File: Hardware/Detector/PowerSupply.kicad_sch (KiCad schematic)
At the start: 3 parts

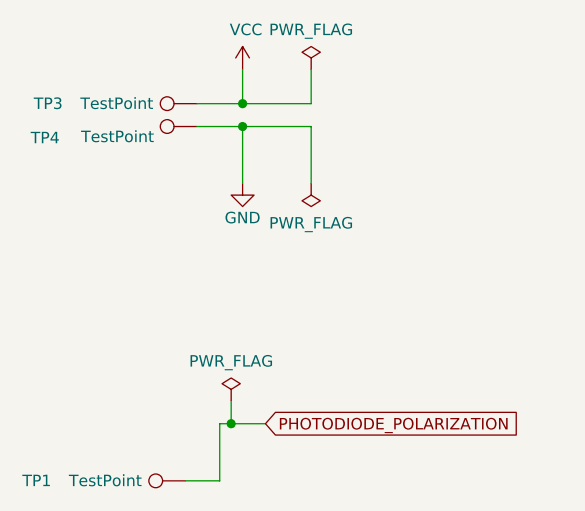
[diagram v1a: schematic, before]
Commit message: further implementation of low cost version
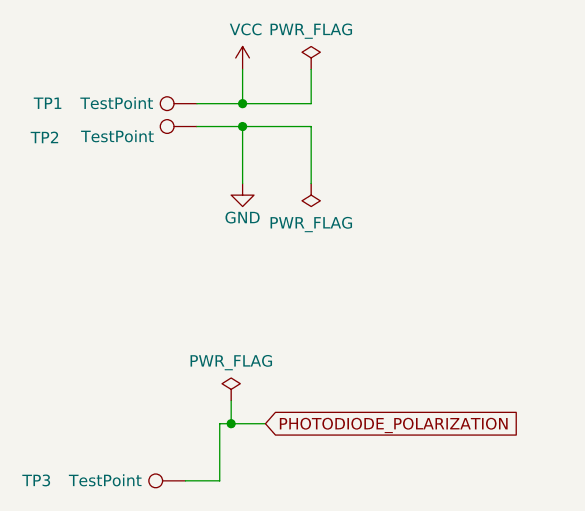
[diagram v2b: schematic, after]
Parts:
- renumbered TP3 to TP1, TP4 to TP2, TP1 to TP3
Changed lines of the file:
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@@
   (symbol (lib_id "power:VCC") (at 95.25 63.5 0) (unit 1)
     (in_bom yes) (on_board yes)
-    (property "Reference" "#PWR021" (id 0) (at 95.25 67.31 0)
+    (property "Reference" "#PWR020" (id 0) (at 95.25 67.31 0)
       (effects (font (size 1.27 1.27)) hide)
     )
@@
   (symbol (lib_id "power:PWR_FLAG") (at 93.98 100.33 0) (unit 1)
     (in_bom yes) (on_board yes)
-    (property "Reference" "#FLG02" (id 0) (at 93.98 98.425 0)
+    (property "Reference" "#FLG04" (id 0) (at 93.98 98.425 0)
       (effects (font (size 1.27 1.27)) hide)
     )
@@
   (symbol (lib_id "power:PWR_FLAG") (at 102.87 63.5 0) (unit 1)
     (in_bom yes) (on_board yes)
-    (property "Reference" "#FLG03" (id 0) (at 102.87 61.595 0)
+    (property "Reference" "#FLG02" (id 0) (at 102.87 61.595 0)
       (effects (font (size 1.27 1.27)) hide)
     )
@@
   (symbol (lib_id "power:PWR_FLAG") (at 102.87 76.2 180) (unit 1)
     (in_bom yes) (on_board yes)
-    (property "Reference" "#FLG04" (id 0) (at 102.87 78.105 0)
+    (property "Reference" "#FLG03" (id 0) (at 102.87 78.105 0)
       (effects (font (size 1.27 1.27)) hide)
     )
@@
   (symbol (lib_id "Connector:TestPoint") (at 88.9 109.22 90) (unit 1)
     (in_bom yes) (on_board yes)
-    (property "Reference" "TP1" (id 0) (at 72.39 109.22 90))
+    (property "Reference" "TP3" (id 0) (at 72.39 109.22 90))
     (property "Value" "TestPoint" (id 1) (at 80.01 109.22 90))
     (property "Footprint" "TestPoint:TestPoint_THTPad_D2.5mm_Drill1.2mm" (id 2) (at 88.9 104.14 0)
@@
   (symbol (lib_id "Connector:TestPoint") (at 90.17 67.31 90) (unit 1)
     (in_bom yes) (on_board yes)
-    (property "Reference" "TP3" (id 0) (at 73.66 67.31 90))
+    (property "Reference" "TP1" (id 0) (at 73.66 67.31 90))
     (property "Value" "TestPoint" (id 1) (at 81.28 67.31 90))
     (property "Footprint" "TestPoint:TestPoint_THTPad_D2.5mm_Drill1.2mm" (id 2) (at 90.17 62.23 0)
@@
   (symbol (lib_id "Connector:TestPoint") (at 90.17 69.85 90) (unit 1)
     (in_bom yes) (on_board yes)
-    (property "Reference" "TP4" (id 0) (at 74.93 71.12 90)
+    (property "Reference" "TP2" (id 0) (at 74.93 71.12 90)
       (effects (font (size 1.27 1.27)) (justify left))
     )
@@
   (symbol (lib_id "power:GND") (at 95.25 76.2 0) (unit 1)
     (in_bom yes) (on_board yes)
-    (property "Reference" "#PWR022" (id 0) (at 95.25 82.55 0)
+    (property "Reference" "#PWR021" (id 0) (at 95.25 82.55 0)
       (effects (font (size 1.27 1.27)) hide)
     )
